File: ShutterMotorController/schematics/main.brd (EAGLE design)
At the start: 100 x 75 mm, 51 parts, among them IC1 MC34063AD, IC2 ULN2003AD, IC3 78L05SMD, J1 SCREW-TERMINAL-2PIN, J2 SCREW-TERMINAL-2PIN, J3 SCREW-TERMINAL-2PIN, J4 SCREW-TERMINAL-2PIN, J5 PWR_IN, K1 35701331, K2 35701331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

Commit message: SMC: fix screw terminal pin pitch; route +3.3V to DS18B20 differently
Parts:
- moved C8 6.38 mm to (73.7, 69.8), turned to 0 degrees
- moved R10 6.38 mm to (73.7, 63.5), turned to 180 degrees
- moved U$1 3.42 mm to (76.2, 65.4), turned to 180 degrees
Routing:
- net +3V3: track 130.2 -> 136.4 mm
- net ESP_DS18B20_DQ: track 23.0 -> 21.3 mm
- net N$16: track 16.9 -> 15.9 mm

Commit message: SMC: add indicator LED
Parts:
- added LED7: Activity, led:LED5MM
- added R14: 150, rcl:R1206
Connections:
- new net ESP_IND_LED: R14.2, X1.4
- new net N$27: LED7.A, R14.1
- net GND: now also LED7.K
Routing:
- net ESP_IND_LED: track 0.00 -> 15.3 mm, vias 0 -> 1
- net N$27: track 0.00 -> 6.18 mm
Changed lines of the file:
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@@
 <?xml version="1.0" encoding="utf-8"?>
 <!DOCTYPE eagle SYSTEM "eagle.dtd">
-<eagle version="8.5.1">
+<eagle version="8.6.1">
 <drawing>
 <settings>
@@
 <attribute name="SPICEPREFIX" value="C" x="55.88" y="43.815" size="1.9304" layer="28" rot="MR0" display="off"/>
 </element>
+<element name="LED7" library="led" library_urn="urn:adsk.eagle:library:259" package="LED5MM" package3d_urn="urn:adsk.eagle:package:15799/2" value="Activity" x="93.345" y="60.96"/>
+<element name="R14" library="rcl" library_urn="urn:adsk.eagle:library:334" package="R1206" package3d_urn="urn:adsk.eagle:package:23540/2" value="150" x="87.63" y="57.15" rot="MR0">
+<attribute name="SPICEPREFIX" value="R" x="87.63" y="57.15" size="1.778" layer="28" rot="MR0" display="off"/>
+</element>
 </elements>
 <signals>
@@
 <contactref element="R13" pad="1"/>
 <contactref element="C9" pad="1"/>
+<contactref element="LED7" pad="K"/>
 </signal>
 <signal name="N$5">
@@
 <wire x1="74.295" y1="34.925" x2="74.295" y2="36.678" width="0.6096" layer="16"/>
 </signal>
+<signal name="N$27">
+<contactref element="R14" pad="1"/>
+<contactref element="LED7" pad="A"/>
+<wire x1="90.17" y1="60.96" x2="92.075" y2="60.96" width="0.6096" layer="16"/>
+<wire x1="89.052" y1="57.15" x2="89.052" y2="59.842" width="0.6096" layer="16"/>
+<wire x1="89.052" y1="59.842" x2="90.17" y2="60.96" width="0.6096" layer="16"/>
+</signal>
+<signal name="ESP_IND_LED">
+<contactref element="R14" pad="2"/>
+<contactref element="X1" pad="4"/>
+<wire x1="81.685" y1="46.235" x2="81.685" y2="56.92" width="0.6096" layer="1"/>
+<wire x1="81.685" y1="56.92" x2="81.915" y2="57.15" width="0.6096" layer="1"/>
+<via x="81.915" y="57.15" extent="1-16" drill="0.9" diameter="1.6"/>
+<wire x1="81.915" y1="57.15" x2="86.208" y2="57.15" width="0.6096" layer="16"/>
+</signal>
 </signals>

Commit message: SMC: add ADC header to the PCB
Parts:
- added C10: 100n, rcl:C1206
- added JP2: ADC, pinhead:1X03
- moved LED7 34.7 mm to (59.7, 69.2), turned to 90 degrees
- moved R14 27.6 mm to (61.0, 64.1), turned to 180 degrees
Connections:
- new net ESP_ADC: JP2.3, X1.2
- net +3V3: now also C10.2, JP2.1
- net GND: now also C10.1, JP2.2
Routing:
- net ESP_ADC: track 0.00 -> 22.3 mm, vias 0 -> 1
- net +3V3: track 136.4 -> 155.9 mm, vias 2 -> 3
- net ESP_IND_LED: track 15.3 -> 34.4 mm
- net N$27: track 6.18 -> 3.87 mm
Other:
- board text added: "ADC"
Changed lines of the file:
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@@
 <grid distance="25" unitdist="mil" unit="mm" style="lines" multiple="1" display="no" altdistance="5" altunitdist="mil" altunit="mil"/>
 <layers>
-<layer number="1" name="Top" color="4" fill="1" visible="yes" active="yes"/>
+<layer number="1" name="Top" color="4" fill="1" visible="no" active="yes"/>
 <layer number="16" name="Bottom" color="1" fill="1" visible="yes" active="yes"/>
 <layer number="17" name="Pads" color="2" fill="1" visible="yes" active="yes"/>
@@
 <text x="78.74" y="11.43" size="1.6764" layer="1" font="vector" ratio="15" rot="R90">3.3V</text>
 <text x="40.64" y="1.905" size="1.9304" layer="1" font="vector" ratio="15">Shutter Motor Controller - ToMikaa - 2018</text>
+<text x="88.265" y="67.31" size="1.6764" layer="1" font="vector" ratio="15" rot="R90">3.3V</text>
+<text x="93.345" y="67.31" size="1.6764" layer="1" font="vector" ratio="15" rot="R90">ADC</text>
+<text x="90.805" y="67.31" size="1.6764" layer="1" font="vector" ratio="15" rot="R90">GND</text>
 </plain>
 <attributes>
@@
 <attribute name="SPICEPREFIX" value="C" x="55.88" y="43.815" size="1.9304" layer="28" rot="MR0" display="off"/>
 </element>
-<element name="LED7" library="led" library_urn="urn:adsk.eagle:library:259" package="LED5MM" package3d_urn="urn:adsk.eagle:package:15799/2" value="Activity" x="93.345" y="60.96"/>
-<element name="R14" library="rcl" library_urn="urn:adsk.eagle:library:334" package="R1206" package3d_urn="urn:adsk.eagle:package:23540/2" value="150" x="87.63" y="57.15" rot="MR0">
-<attribute name="SPICEPREFIX" value="R" x="87.63" y="57.15" size="1.778" layer="28" rot="MR0" display="off"/>
+<element name="LED7" library="led" library_urn="urn:adsk.eagle:library:259" package="LED5MM" package3d_urn="urn:adsk.eagle:package:15799/2" value="Activity" x="59.69" y="69.215" rot="R90"/>
+<element name="R14" library="rcl" library_urn="urn:adsk.eagle:library:334" package="R1206" package3d_urn="urn:adsk.eagle:package:23540/2" value="150" x="60.96" y="64.135" rot="MR180">
+<attribute name="SPICEPREFIX" value="R" x="60.96" y="64.135" size="1.778" layer="28" rot="MR180" display="off"/>
+</element>
+<element name="JP2" library="pinhead" library_urn="urn:adsk.eagle:library:325" package="1X03" package3d_urn="urn:adsk.eagle:package:22458/2" value="ADC" x="90.17" y="64.135"/>
+<element name="C10" library="rcl" library_urn="urn:adsk.eagle:library:334" package="C1206" package3d_urn="urn:adsk.eagle:package:23618/2" value="100n" x="88.265" y="59.055" rot="MR0">
+<attribute name="SPICEPREFIX" value="C" x="88.265" y="59.055" size="1.778" layer="28" rot="MR0" display="off"/>
 </element>
 </elements>
@@
 <contactref element="C9" pad="1"/>
 <contactref element="LED7" pad="K"/>
+<contactref element="C10" pad="1"/>
+<contactref element="JP2" pad="2"/>
 </signal>
 <signal name="N$5">
@@
 <wire x1="49.66" y1="13.97" x2="50.165" y2="14.475" width="1.27" layer="1"/>
 <wire x1="50.165" y1="14.475" x2="50.165" y2="19.81" width="1.524" layer="1"/>
-<wire x1="83.685" y1="46.235" x2="83.685" y2="44.315" width="0.6096" layer="1"/>
-<wire x1="83.685" y1="44.315" x2="82.55" y2="43.18" width="0.6096" layer="1"/>
-<wire x1="82.55" y1="43.18" x2="73.66" y2="43.18" width="0.6096" layer="1"/>
+<wire x1="83.685" y1="46.235" x2="83.685" y2="44.315" width="0.8128" layer="1"/>
+<wire x1="83.685" y1="44.315" x2="82.55" y2="43.18" width="0.8128" layer="1"/>
+<wire x1="82.55" y1="43.18" x2="73.66" y2="43.18" width="0.8128" layer="1"/>
 <wire x1="73.66" y1="43.18" x2="73.595" y2="43.245" width="0.6096" layer="1"/>
 <wire x1="70.485" y1="40.135" x2="67.18" y2="40.135" width="1.27" layer="1"/>
@@
 <wire x1="71.755" y1="66.675" x2="71.755" y2="69.345" width="0.8128" layer="1"/>
 <wire x1="71.755" y1="69.345" x2="72.26" y2="69.85" width="0.8128" layer="1"/>
+<contactref element="C10" pad="2"/>
+<contactref element="JP2" pad="1"/>
+<wire x1="87.63" y1="64.135" x2="86.865" y2="63.37" width="0.8128" layer="16"/>
+<wire x1="86.865" y1="63.37" x2="86.865" y2="59.055" width="0.8128" layer="16"/>
+<wire x1="83.685" y1="46.235" x2="83.685" y2="53.84" width="0.8128" layer="1"/>
+<wire x1="83.685" y1="53.84" x2="85.09" y2="55.245" width="0.8128" layer="1"/>
+<via x="85.09" y="55.245" extent="1-16" drill="0.9" diameter="1.6"/>
+<wire x1="85.09" y1="55.245" x2="86.865" y2="57.02" width="0.8128" layer="16"/>
+<wire x1="86.865" y1="57.02" x2="86.865" y2="59.055" width="0.8128" layer="16"/>
 </signal>
 <signal name="N$2">
@@
 <wire x1="83.685" y1="28.71" x2="83.82" y2="27.94" width="0.6096" layer="1"/>
 <via x="83.82" y="27.94" extent="1-16" drill="0.9" diameter="1.6"/>
-<wire x1="83.82" y1="27.94" x2="83.82" y2="50.8" width="0.6096" layer="16"/>
+<wire x1="83.82" y1="27.94" x2="83.82" y2="46.355" width="0.6096" layer="16"/>
+<wire x1="83.82" y1="46.355" x2="83.82" y2="50.8" width="0.6096" layer="16"/>
 <wire x1="83.82" y1="50.8" x2="81.28" y2="53.34" width="0.6096" layer="16"/>
 <wire x1="81.28" y1="53.34" x2="70.485" y2="53.34" width="0.6096" layer="16"/>
@@
 <contactref element="R14" pad="1"/>
 <contactref element="LED7" pad="A"/>
-<wire x1="90.17" y1="60.96" x2="92.075" y2="60.96" width="0.6096" layer="16"/>
-<wire x1="89.052" y1="57.15" x2="89.052" y2="59.842" width="0.6096" layer="16"/>
-<wire x1="89.052" y1="59.842" x2="90.17" y2="60.96" width="0.6096" layer="16"/>
+<wire x1="59.69" y1="67.945" x2="59.538" y2="67.793" width="0.6096" layer="16"/>
+<wire x1="59.538" y1="67.793" x2="59.538" y2="64.135" width="0.6096" layer="16"/>
 </signal>
 <signal name="ESP_IND_LED">
 <contactref element="R14" pad="2"/>
 <contactref element="X1" pad="4"/>
-<wire x1="81.685" y1="46.235" x2="81.685" y2="56.92" width="0.6096" layer="1"/>
-<wire x1="81.685" y1="56.92" x2="81.915" y2="57.15" width="0.6096" layer="1"/>
-<via x="81.915" y="57.15" extent="1-16" drill="0.9" diameter="1.6"/>
-<wire x1="81.915" y1="57.15" x2="86.208" y2="57.15" width="0.6096" layer="16"/>
+<wire x1="81.685" y1="46.235" x2="81.685" y2="59.285" width="0.6096" layer="1"/>
+<wire x1="81.685" y1="59.285" x2="80.645" y2="60.325" width="0.6096" layer="1"/>
+<via x="80.645" y="60.325" extent="1-16" drill="0.9" diameter="1.6"/>
+<wire x1="80.645" y1="60.325" x2="66.192" y2="60.325" width="0.6096" layer="16"/>
+<wire x1="66.192" y1="60.325" x2="62.382" y2="64.135" width="0.6096" layer="16"/>
+</signal>
+<signal name="ESP_ADC">
+<contactref element="X1" pad="2"/>
+<contactref element="JP2" pad="3"/>
+<wire x1="85.685" y1="46.235" x2="85.685" y2="51.395" width="0.6096" layer="1"/>
+<wire x1="85.685" y1="51.395" x2="88.265" y2="53.975" width="0.6096" layer="1"/>
+<via x="88.265" y="53.975" extent="1-16" drill="0.9" diameter="1.6"/>
+<wire x1="88.265" y1="53.975" x2="90.805" y2="53.975" width="0.6096" layer="16"/>
+<wire x1="90.805" y1="53.975" x2="92.71" y2="55.88" width="0.6096" layer="16"/>
+<wire x1="92.71" y1="55.88" x2="92.71" y2="64.135" width="0.6096" layer="16"/>
 </signal>
 </signals>

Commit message: SMC: fix DRC errors of board design
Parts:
- removed U$1: DS1820TO92, Ava:DS1820
- added JP3: (no value), pinhead:1X03
- moved R10 1.42 mm to (72.4, 62.9)
- moved C8 0.64 mm to (73.7, 70.5)
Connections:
- net +3V3: now also JP3.1; no longer U$1.VDD
- net ESP_DS18B20_DQ: now also JP3.2; no longer U$1.DQ
- net GND: now also JP3.3; no longer U$1.GND
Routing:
- net ESP_RELAY1: track 53.1 -> 54.5 mm
- net N$26: track 12.6 -> 13.9 mm
- net ESP_RST: track 35.3 -> 36.4 mm

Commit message: SMC: fix screw-terminal pin pitch and drawing
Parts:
- moved J4 4.79 mm to (9.93, 41.6)
- moved J1 4.73 mm to (9.93, 62.6)
- moved J3 1.66 mm to (9.93, 48.6)
- moved J2 1.60 mm to (9.93, 55.6)
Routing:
- net N$6: track 87.7 -> 73.3 mm
- net N$8: track 65.5 -> 54.0 mm
- net N$13: track 42.3 -> 34.9 mm
- net N$16: track 15.9 -> 11.2 mm
- net N$3: track 42.2 -> 37.9 mm
- net N$15: track 25.1 -> 22.7 mm
- net N$11: track 30.1 -> 28.4 mm
- net N$7: track 30.2 -> 31.6 mm

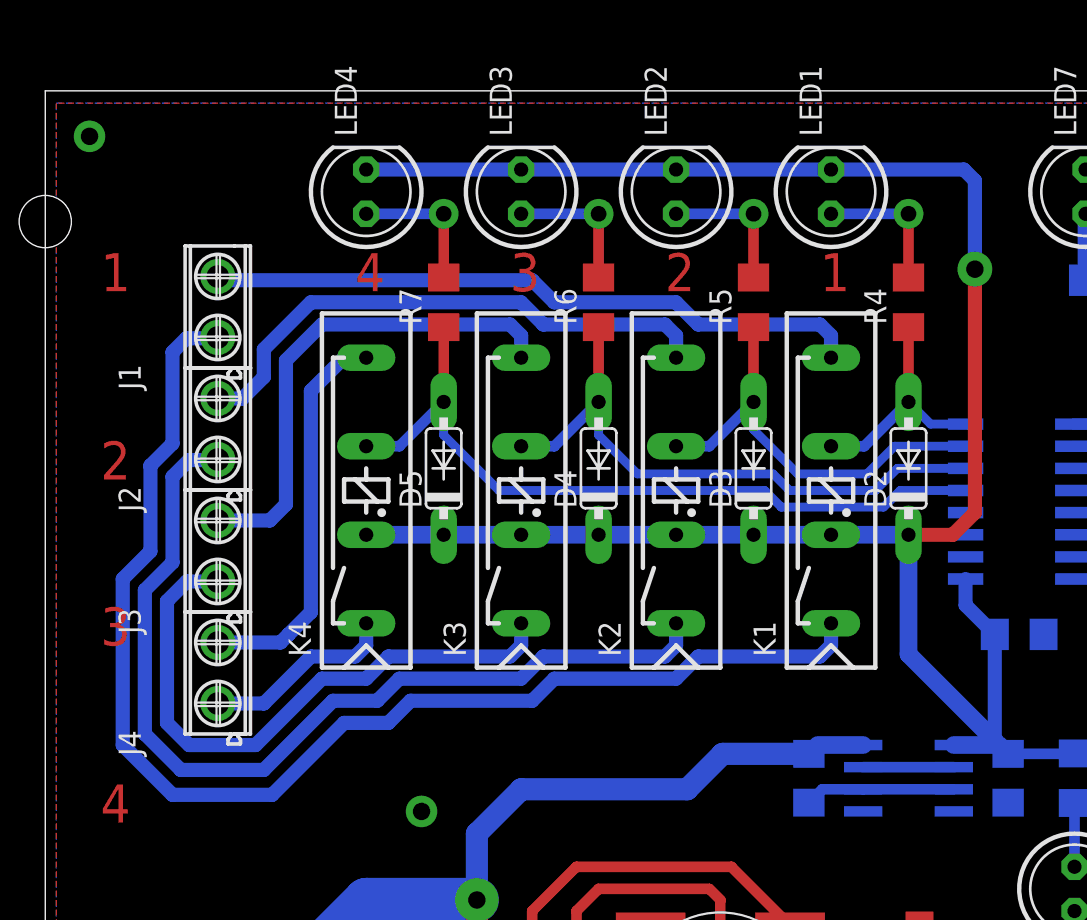
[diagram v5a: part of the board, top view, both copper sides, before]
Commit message: SMC: increase clearance between switched relay tracks
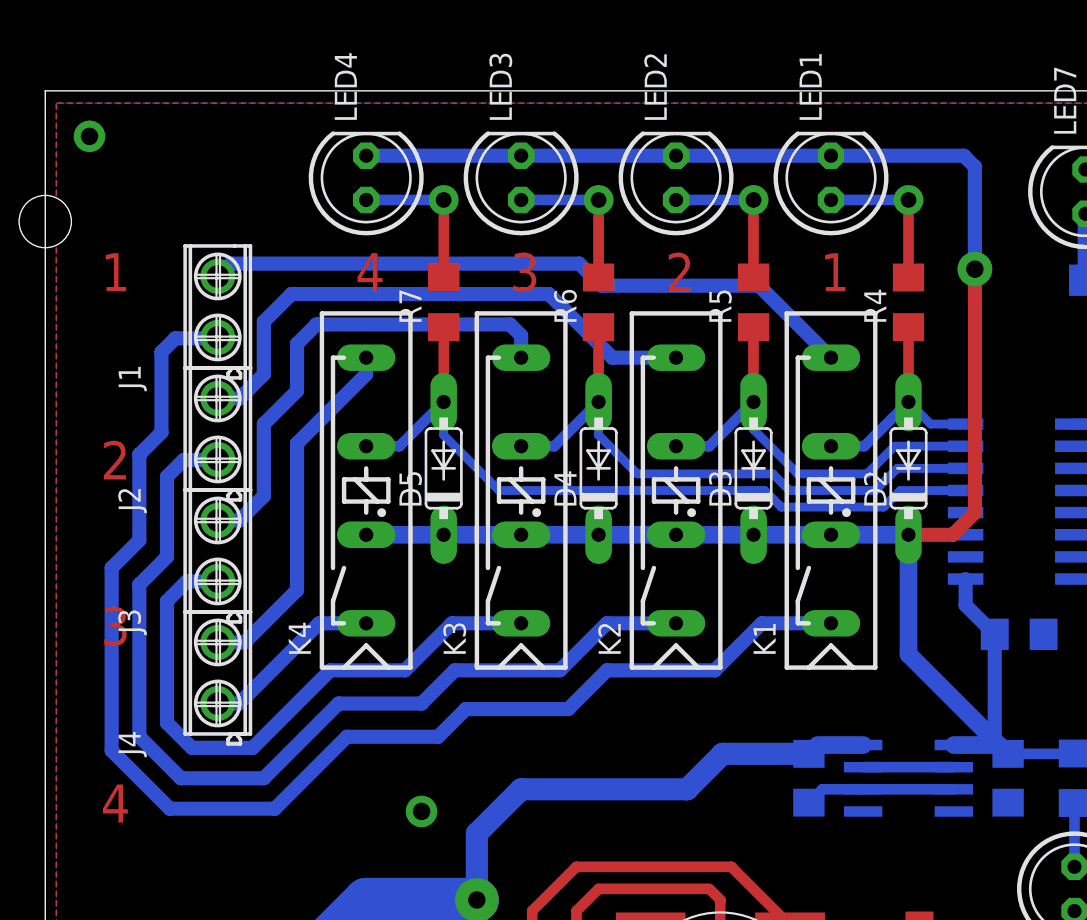
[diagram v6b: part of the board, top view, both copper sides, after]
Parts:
- moved LED1 0.79 mm to (45.1, 70.0)
- moved LED2 0.79 mm to (36.2, 70.0)
- moved LED3 0.79 mm to (27.3, 70.0)
- moved LED4 0.79 mm to (18.4, 70.0)
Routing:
- net N$15: track 22.7 -> 20.8 mm
- net N$6: track 73.3 -> 74.7 mm
- net N$11: track 28.4 -> 27.6 mm
- net N$22: track 8.10 -> 8.90 mm
- net N$21: track 8.10 -> 8.90 mm
- net N$20: track 8.10 -> 8.90 mm
- net N$18: track 8.10 -> 8.90 mm
- net +5V: track 121.0 -> 121.8 mm
- net N$16: track 11.2 -> 10.4 mm
- net N$13: track 34.9 -> 34.2 mm
